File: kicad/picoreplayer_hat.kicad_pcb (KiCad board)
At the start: 2 copper layers, 59.1 x 38.7 mm, 20 parts, among them J1 5v IN, J2 PANEL ON/OFF, J3 Raspberry_Pi3, J4 DISPLAY, J5 DAC, J6 PICORE ENCODER & BTN, K2 Relay_HFD2_bistabile, Q1 2N3904, Q2 2N3904, SW1 ON/OFF, SW2 HARD STOP

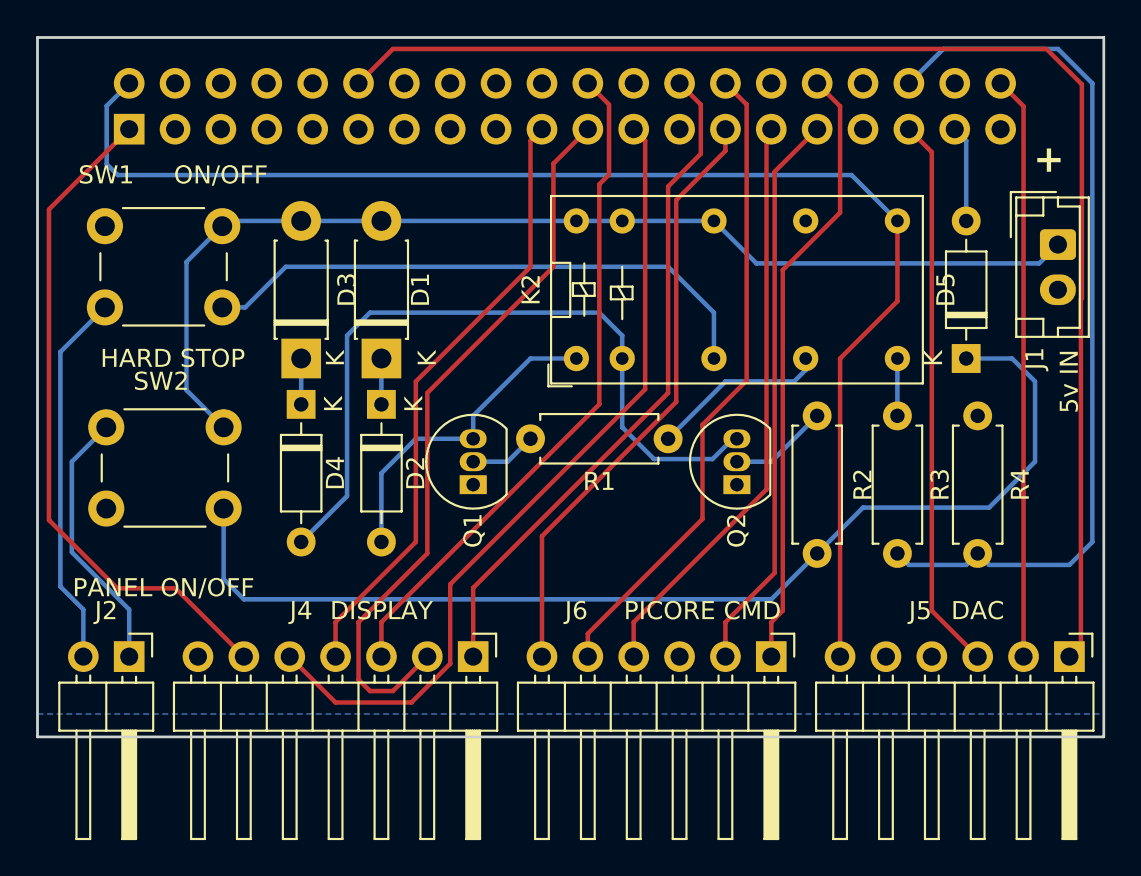
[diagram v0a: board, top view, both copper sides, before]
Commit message: increased PCB tracks for power section
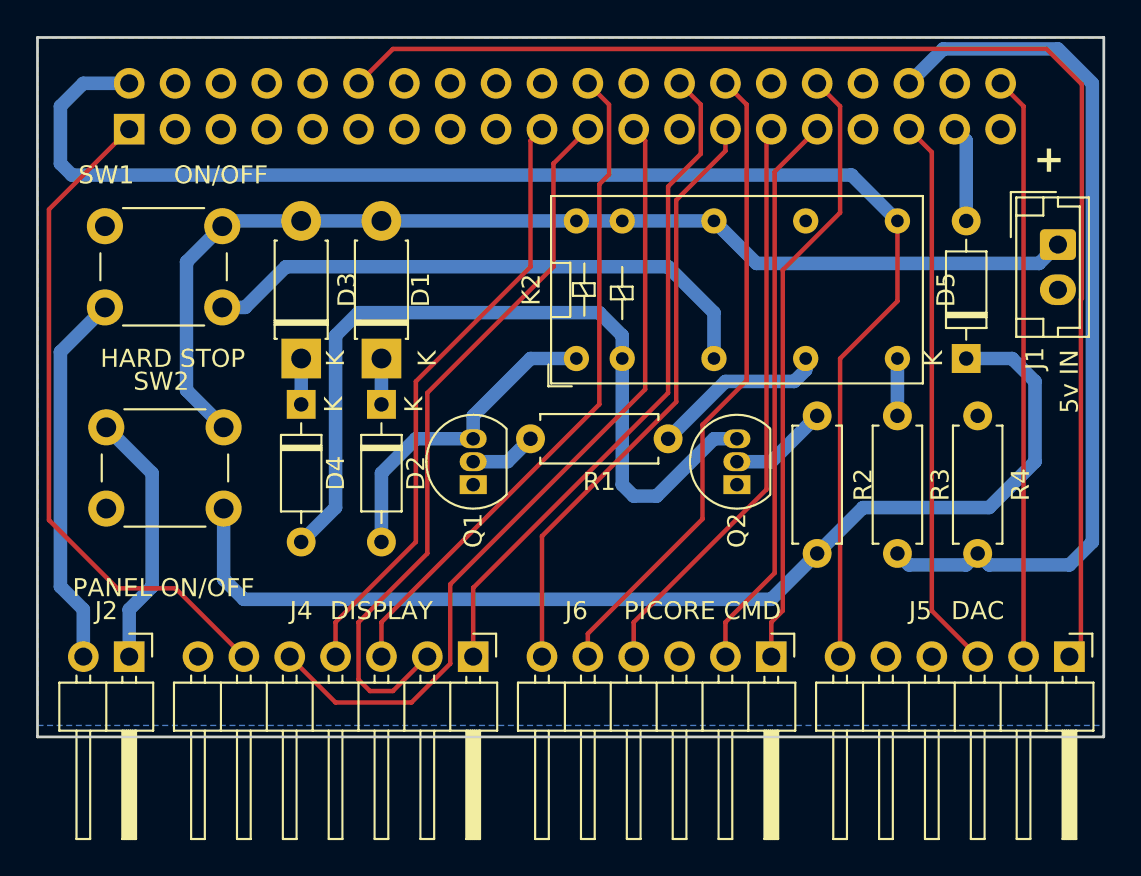
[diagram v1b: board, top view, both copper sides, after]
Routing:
- net /DAC_VCC: track 75.5 -> 80.6 mm
- net Net-(D4-A): track 41.4 -> 45.3 mm
- net +5V: track 75.4 -> 74.9 mm

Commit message: changed diode model to 1N4007 and added pulldown resistors to the transistor base
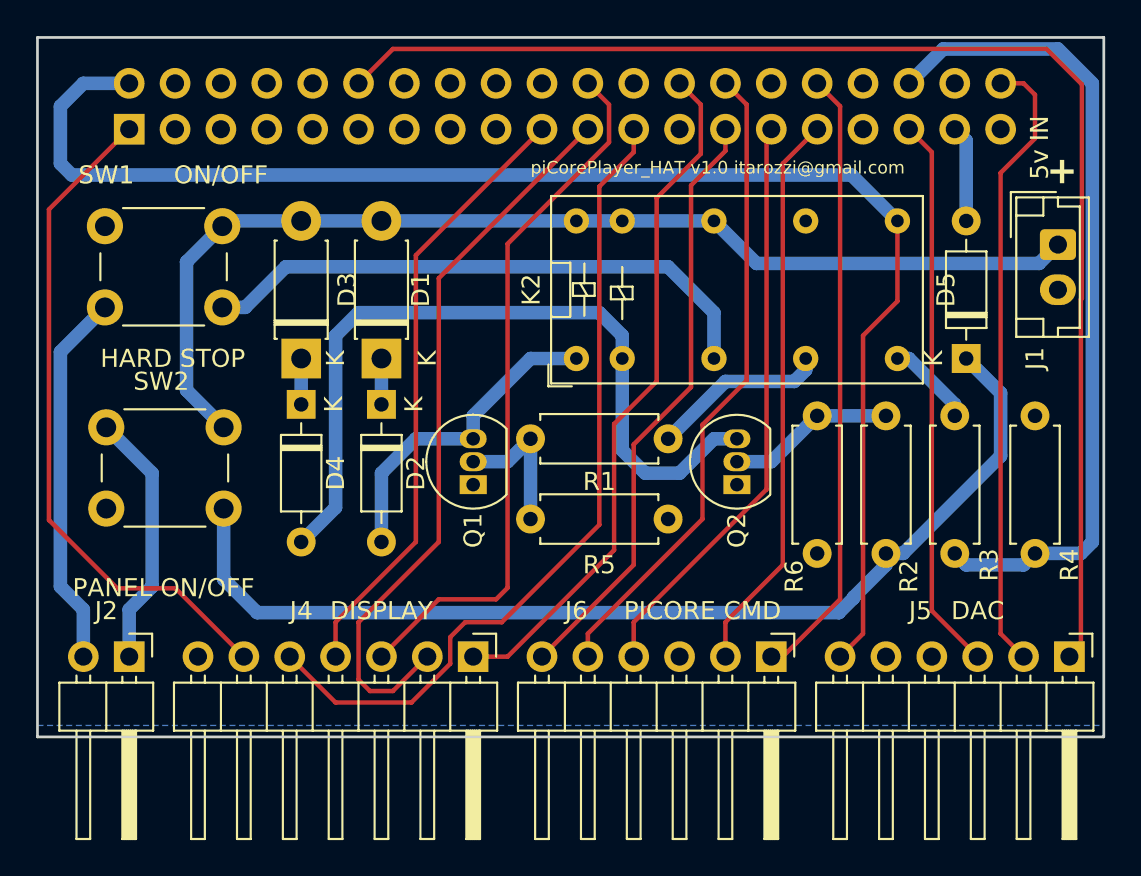
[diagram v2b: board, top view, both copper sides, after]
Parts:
- added R5: 10k, Resistor_THT:R_Axial_DIN0207_L6.3mm_D2.5mm_P7.62mm_Horizontal, F.Cu at (139.1, 93.3)
- added R6: 10k, Resistor_THT:R_Axial_DIN0207_L6.3mm_D2.5mm_P7.62mm_Horizontal, F.Cu at (154.9, 95.2)
- moved R2 3.81 mm to (158.8, 95.2)
- moved R3 3.18 mm to (162.6, 87.6)
- moved R4 3.17 mm to (167.0, 87.6)
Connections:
- K2 pad 9: Net-(K2-Pad9) -> Net-(D5-K)
- R3 pad 1: Net-(K2-Pad9) -> Net-(D5-K)
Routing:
- net Net-(Q1-B): track 3.70 -> 8.15 mm
- net Net-(Q2-B): track 5.50 -> 9.31 mm
- net /SHUTDOWN_CMD: track 49.2 -> 45.5 mm
- net Net-(K2-Pad9): track 3.17 -> 0.00 mm
- net /DAC_DATA: track 32.3 -> 34.6 mm
- net Net-(D4-A): track 45.3 -> 43.2 mm
- net /DISPLAY_RST: track 37.5 -> 39.3 mm
- net Net-(D5-K): track 61.2 -> 62.7 mm
- net /DISPLAY_CS: track 37.5 -> 38.6 mm
- net /DISPLAY_SCL: track 45.2 -> 45.8 mm
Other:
- board text added: "piCorePlayer_HAT v1.0 itarozzi@gmail.com"

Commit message: changed symbols and footprint for 1N4007
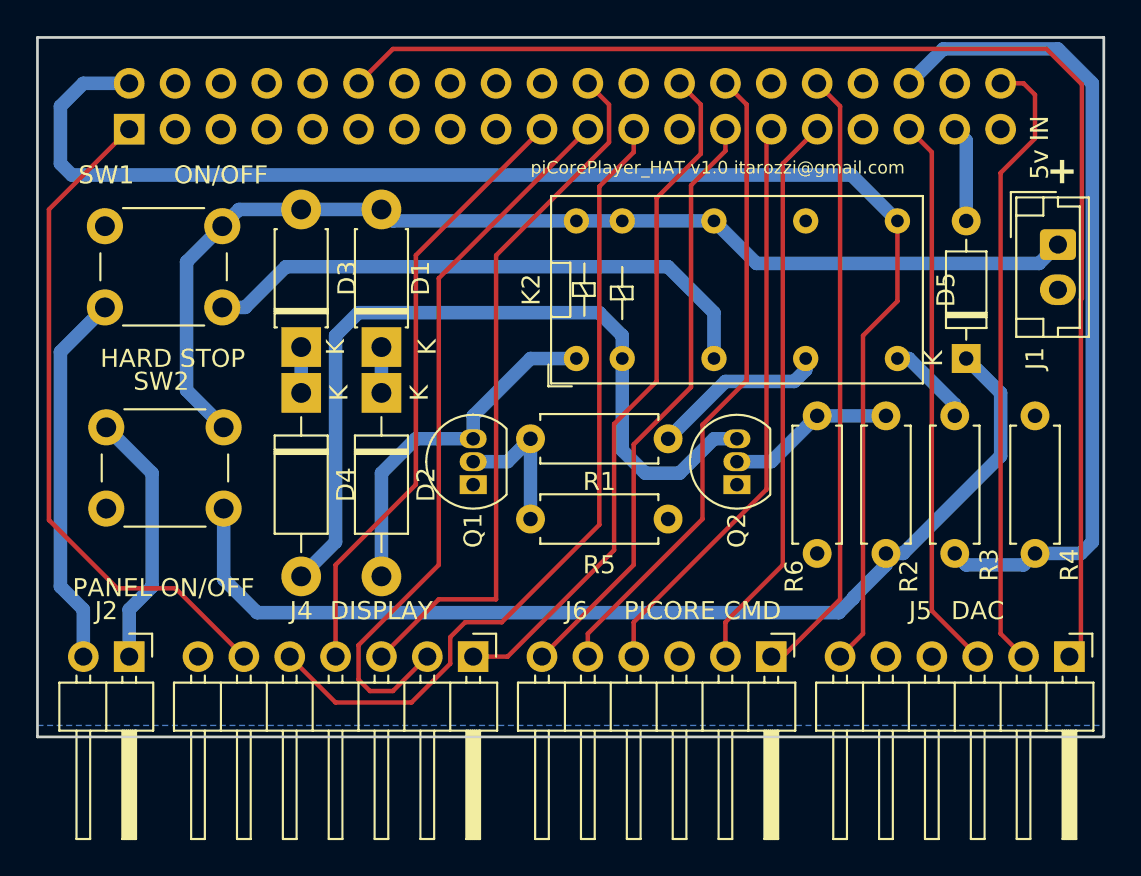
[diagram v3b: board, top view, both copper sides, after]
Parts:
- D2, D4: value 1N4148 -> 1N4007; footprint Diode_THT:D_DO-35_SOD27_P7.62mm_Horizontal -> Diode_THT:D_DO-41_SOD81_P10.16mm_Horizontal
- moved D1 0.64 mm to (130.8, 83.8)
- moved D2 0.64 mm to (130.8, 86.4)
- moved D3 0.64 mm to (126.4, 83.8)
- moved D4 0.64 mm to (126.4, 86.4)
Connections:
- K2 pad 9: Net-(D5-K) -> Net-(K2-Pad9)
- R3 pad 1: Net-(D5-K) -> Net-(K2-Pad9)
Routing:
- net Net-(K2-Pad9): track 0.00 -> 4.86 mm
- net Net-(D5-K): track 62.7 -> 57.9 mm
- net Net-(D4-A): track 43.2 -> 45.1 mm
- net Net-(D2-A): track 18.0 -> 19.9 mm
- net Net-(D3-K): track 2.54 -> 3.18 mm
- net Net-(D1-K): track 2.54 -> 3.18 mm
- net +5V: track 74.9 -> 75.4 mm
